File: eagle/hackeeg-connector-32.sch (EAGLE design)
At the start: 58 parts

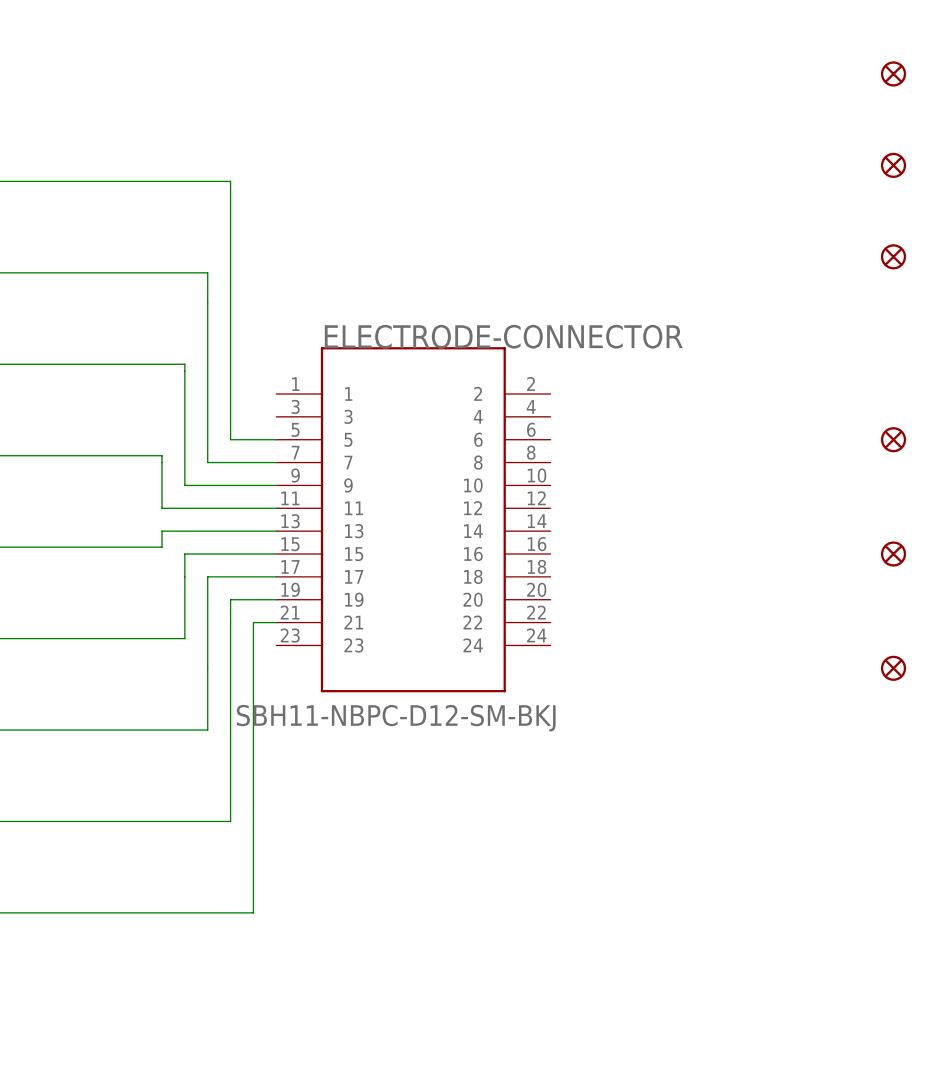
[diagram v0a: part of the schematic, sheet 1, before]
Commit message: connected IN1-8N to ground
- for cable noise reduction
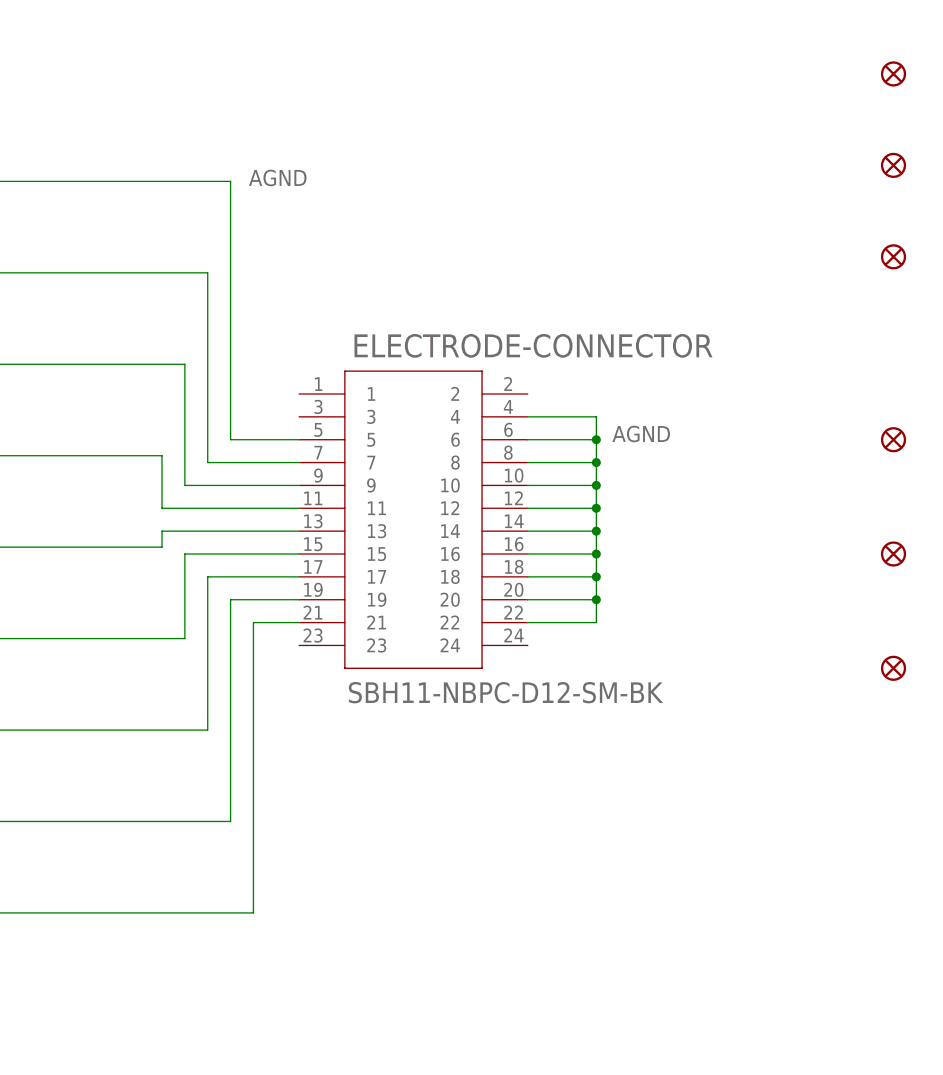
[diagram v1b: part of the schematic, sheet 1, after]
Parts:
- ELECTRODE-CONNECTOR, ELECTRODE-CONNECTOR1, ELECTRODE-CONNECTOR2, ELECTRODE-CONNECTOR3: value SBH11-NBPC-D12-SM-BKJ -> SBH11-NBPC-D12-SM-BK; device SBH11-NBPC-D12-SM-BK:SBH11-NBPC-D12-SM-BKJ -> SBH11-NBPC-D12-SM-BK:SBH11-NBPC-D12-SM-BK
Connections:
- removed net N$1: AGND.SIGNAL, ELECTRODE-CONNECTOR.5
- removed net N$10: AGND1.SIGNAL, ELECTRODE-CONNECTOR1.5
- removed net N$19: AGND2.SIGNAL, ELECTRODE-CONNECTOR2.5
- removed net N$28: AGND3.SIGNAL, ELECTRODE-CONNECTOR3.5
- new net AGND: AGND.SIGNAL, AGND1.SIGNAL, AGND2.SIGNAL, AGND3.SIGNAL, ELECTRODE-CONNECTOR.10, ELECTRODE-CONNECTOR.12, ELECTRODE-CONNECTOR.14, ELECTRODE-CONNECTOR.16, ELECTRODE-CONNECTOR.18, ELECTRODE-CONNECTOR.20, ELECTRODE-CONNECTOR.22, ELECTRODE-CONNECTOR.4, ELECTRODE-CONNECTOR.5, ELECTRODE-CONNECTOR.6, ELECTRODE-CONNECTOR.8, ELECTRODE-CONNECTOR1.10, ELECTRODE-CONNECTOR1.12, ELECTRODE-CONNECTOR1.14, ELECTRODE-CONNECTOR1.16, ELECTRODE-CONNECTOR1.18, ELECTRODE-CONNECTOR1.20, ELECTRODE-CONNECTOR1.22, ELECTRODE-CONNECTOR1.4, ELECTRODE-CONNECTOR1.5, ELECTRODE-CONNECTOR1.6, ELECTRODE-CONNECTOR1.8, ELECTRODE-CONNECTOR2.10, ELECTRODE-CONNECTOR2.12, ELECTRODE-CONNECTOR2.14, ELECTRODE-CONNECTOR2.16, ELECTRODE-CONNECTOR2.18, ELECTRODE-CONNECTOR2.20, ELECTRODE-CONNECTOR2.22, ELECTRODE-CONNECTOR2.4, ELECTRODE-CONNECTOR2.5, ELECTRODE-CONNECTOR2.6, ELECTRODE-CONNECTOR2.8, ELECTRODE-CONNECTOR3.10, ELECTRODE-CONNECTOR3.12, ELECTRODE-CONNECTOR3.14, ELECTRODE-CONNECTOR3.16, ELECTRODE-CONNECTOR3.18, ELECTRODE-CONNECTOR3.20, ELECTRODE-CONNECTOR3.22, ELECTRODE-CONNECTOR3.4, ELECTRODE-CONNECTOR3.5, ELECTRODE-CONNECTOR3.6, ELECTRODE-CONNECTOR3.8

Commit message: updated libraries to current
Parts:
- AGND, AGND1, AGND2, AGND3, IN1P, IN1P1, IN1P2, IN1P3, IN2P, IN2P1, IN2P2, IN2P3, IN3P, IN3P1, IN3P2, IN3P3, IN4P, IN4P1, IN4P2, IN4P3, IN5P, IN5P1, IN5P2, IN5P3, IN6P, IN6P1, IN6P2, IN6P3, IN7P, IN7P1, IN7P2, IN7P3, IN8P, IN8P1, IN8P2, IN8P3: value PO37729HEX-100 -> PO37729HEX-110; device po-37729:PO37729HEX-100 -> po-37729:PO37729HEX-110
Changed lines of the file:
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@@
 </classes>
 <parts>
-<part name="IN1P" library="po-37729" deviceset="PO37729" device="HEX-100"/>
+<part name="IN1P" library="po-37729" deviceset="PO37729" device="HEX-110"/>
 <part name="FRAME1" library="SparkFun-Aesthetics" library_urn="urn:adsk.eagle:library:507" deviceset="FRAME-LETTER" device="" package3d_urn="urn:adsk.eagle:package:37121/1"/>
 <part name="ELECTRODE-CONNECTOR" library="SBH11-NBPC-D12-SM-BK" deviceset="SBH11-NBPC-D12-SM-BK" device=""/>
 <part name="U$13" library="creative-commons" deviceset="CC-BY-SA" device=""/>
-<part name="IN2P" library="po-37729" deviceset="PO37729" device="HEX-100"/>
-<part name="IN3P" library="po-37729" deviceset="PO37729" device="HEX-100"/>
-<part name="IN4P" library="po-37729" deviceset="PO37729" device="HEX-100"/>
-<part name="IN5P" library="po-37729" deviceset="PO37729" device="HEX-100"/>
-<part name="IN6P" library="po-37729" deviceset="PO37729" device="HEX-100"/>
-<part name="IN7P" library="po-37729" deviceset="PO37729" device="HEX-100"/>
-<part name="AGND" library="po-37729" deviceset="PO37729" device="HEX-100"/>
-<part name="IN8P" library="po-37729" deviceset="PO37729" device="HEX-100"/>
+<part name="IN2P" library="po-37729" deviceset="PO37729" device="HEX-110"/>
+<part name="IN3P" library="po-37729" deviceset="PO37729" device="HEX-110"/>
+<part name="IN4P" library="po-37729" deviceset="PO37729" device="HEX-110"/>
+<part name="IN5P" library="po-37729" deviceset="PO37729" device="HEX-110"/>
+<part name="IN6P" library="po-37729" deviceset="PO37729" device="HEX-110"/>
+<part name="IN7P" library="po-37729" deviceset="PO37729" device="HEX-110"/>
+<part name="AGND" library="po-37729" deviceset="PO37729" device="HEX-110"/>
+<part name="IN8P" library="po-37729" deviceset="PO37729" device="HEX-110"/>
 <part name="U$1" library="endless-knot" deviceset="ENDLESSKNOT" device="ENDLESSKNOT-MEDIUM"/>
-<part name="IN1P1" library="po-37729" deviceset="PO37729" device="HEX-100"/>
+<part name="IN1P1" library="po-37729" deviceset="PO37729" device="HEX-110"/>
 <part name="FRAME2" library="SparkFun-Aesthetics" library_urn="urn:adsk.eagle:library:507" deviceset="FRAME-LETTER" device="" package3d_urn="urn:adsk.eagle:package:37121/1"/>
 <part name="ELECTRODE-CONNECTOR1" library="SBH11-NBPC-D12-SM-BK" deviceset="SBH11-NBPC-D12-SM-BK" device=""/>
 <part name="U$2" library="creative-commons" deviceset="CC-BY-SA" device=""/>
-<part name="IN2P1" library="po-37729" deviceset="PO37729" device="HEX-100"/>
-<part name="IN3P1" library="po-37729" deviceset="PO37729" device="HEX-100"/>
-<part name="IN4P1" library="po-37729" deviceset="PO37729" device="HEX-100"/>
-<part name="IN5P1" library="po-37729" deviceset="PO37729" device="HEX-100"/>
-<part name="IN6P1" library="po-37729" deviceset="PO37729" device="HEX-100"/>
-<part name="IN7P1" library="po-37729" deviceset="PO37729" device="HEX-100"/>
-<part name="AGND1" library="po-37729" deviceset="PO37729" device="HEX-100"/>
-<part name="IN8P1" library="po-37729" deviceset="PO37729" device="HEX-100"/>
+<part name="IN2P1" library="po-37729" deviceset="PO37729" device="HEX-110"/>
+<part name="IN3P1" library="po-37729" deviceset="PO37729" device="HEX-110"/>
+<part name="IN4P1" library="po-37729" deviceset="PO37729" device="HEX-110"/>
+<part name="IN5P1" library="po-37729" deviceset="PO37729" device="HEX-110"/>
+<part name="IN6P1" library="po-37729" deviceset="PO37729" device="HEX-110"/>
+<part name="IN7P1" library="po-37729" deviceset="PO37729" device="HEX-110"/>
+<part name="AGND1" library="po-37729" deviceset="PO37729" device="HEX-110"/>
+<part name="IN8P1" library="po-37729" deviceset="PO37729" device="HEX-110"/>
 <part name="U$3" library="endless-knot" deviceset="ENDLESSKNOT" device="ENDLESSKNOT-MEDIUM"/>
-<part name="IN1P2" library="po-37729" deviceset="PO37729" device="HEX-100"/>
+<part name="IN1P2" library="po-37729" deviceset="PO37729" device="HEX-110"/>
 <part name="FRAME3" library="SparkFun-Aesthetics" library_urn="urn:adsk.eagle:library:507" deviceset="FRAME-LETTER" device="" package3d_urn="urn:adsk.eagle:package:37121/1"/>
 <part name="ELECTRODE-CONNECTOR2" library="SBH11-NBPC-D12-SM-BK" deviceset="SBH11-NBPC-D12-SM-BK" device=""/>
 <part name="U$4" library="creative-commons" deviceset="CC-BY-SA" device=""/>
-<part name="IN2P2" library="po-37729" deviceset="PO37729" device="HEX-100"/>
-<part name="IN3P2" library="po-37729" deviceset="PO37729" device="HEX-100"/>
-<part name="IN4P2" library="po-37729" deviceset="PO37729" device="HEX-100"/>
-<part name="IN5P2" library="po-37729" deviceset="PO37729" device="HEX-100"/>
-<part name="IN6P2" library="po-37729" deviceset="PO37729" device="HEX-100"/>
-<part name="IN7P2" library="po-37729" deviceset="PO37729" device="HEX-100"/>
-<part name="AGND2" library="po-37729" deviceset="PO37729" device="HEX-100"/>
-<part name="IN8P2" library="po-37729" deviceset="PO37729" device="HEX-100"/>
+<part name="IN2P2" library="po-37729" deviceset="PO37729" device="HEX-110"/>
+<part name="IN3P2" library="po-37729" deviceset="PO37729" device="HEX-110"/>
+<part name="IN4P2" library="po-37729" deviceset="PO37729" device="HEX-110"/>
+<part name="IN5P2" library="po-37729" deviceset="PO37729" device="HEX-110"/>
+<part name="IN6P2" library="po-37729" deviceset="PO37729" device="HEX-110"/>
+<part name="IN7P2" library="po-37729" deviceset="PO37729" device="HEX-110"/>
+<part name="AGND2" library="po-37729" deviceset="PO37729" device="HEX-110"/>
+<part name="IN8P2" library="po-37729" deviceset="PO37729" device="HEX-110"/>
 <part name="U$5" library="endless-knot" deviceset="ENDLESSKNOT" device="ENDLESSKNOT-MEDIUM"/>
-<part name="IN1P3" library="po-37729" deviceset="PO37729" device="HEX-100"/>
+<part name="IN1P3" library="po-37729" deviceset="PO37729" device="HEX-110"/>
 <part name="FRAME4" library="SparkFun-Aesthetics" library_urn="urn:adsk.eagle:library:507" deviceset="FRAME-LETTER" device="" package3d_urn="urn:adsk.eagle:package:37121/1"/>
 <part name="ELECTRODE-CONNECTOR3" library="SBH11-NBPC-D12-SM-BK" deviceset="SBH11-NBPC-D12-SM-BK" device=""/>
 <part name="U$6" library="creative-commons" deviceset="CC-BY-SA" device=""/>
-<part name="IN2P3" library="po-37729" deviceset="PO37729" device="HEX-100"/>
-<part name="IN3P3" library="po-37729" deviceset="PO37729" device="HEX-100"/>
-<part name="IN4P3" library="po-37729" deviceset="PO37729" device="HEX-100"/>
-<part name="IN5P3" library="po-37729" deviceset="PO37729" device="HEX-100"/>
-<part name="IN6P3" library="po-37729" deviceset="PO37729" device="HEX-100"/>
-<part name="IN7P3" library="po-37729" deviceset="PO37729" device="HEX-100"/>
-<part name="AGND3" library="po-37729" deviceset="PO37729" device="HEX-100"/>
-<part name="IN8P3" library="po-37729" deviceset="PO37729" device="HEX-100"/>
+<part name="IN2P3" library="po-37729" deviceset="PO37729" device="HEX-110"/>
+<part name="IN3P3" library="po-37729" deviceset="PO37729" device="HEX-110"/>
+<part name="IN4P3" library="po-37729" deviceset="PO37729" device="HEX-110"/>
+<part name="IN5P3" library="po-37729" deviceset="PO37729" device="HEX-110"/>
+<part name="IN6P3" library="po-37729" deviceset="PO37729" device="HEX-110"/>
+<part name="IN7P3" library="po-37729" deviceset="PO37729" device="HEX-110"/>
+<part name="AGND3" library="po-37729" deviceset="PO37729" device="HEX-110"/>
+<part name="IN8P3" library="po-37729" deviceset="PO37729" device="HEX-110"/>
 <part name="U$7" library="endless-knot" deviceset="ENDLESSKNOT" device="ENDLESSKNOT-MEDIUM"/>
 <part name="FD1" library="SparkFun-Aesthetics" library_urn="urn:adsk.eagle:library:507" deviceset="FIDUCIAL" device="1X2" package3d_urn="urn:adsk.eagle:package:37108/1"/>

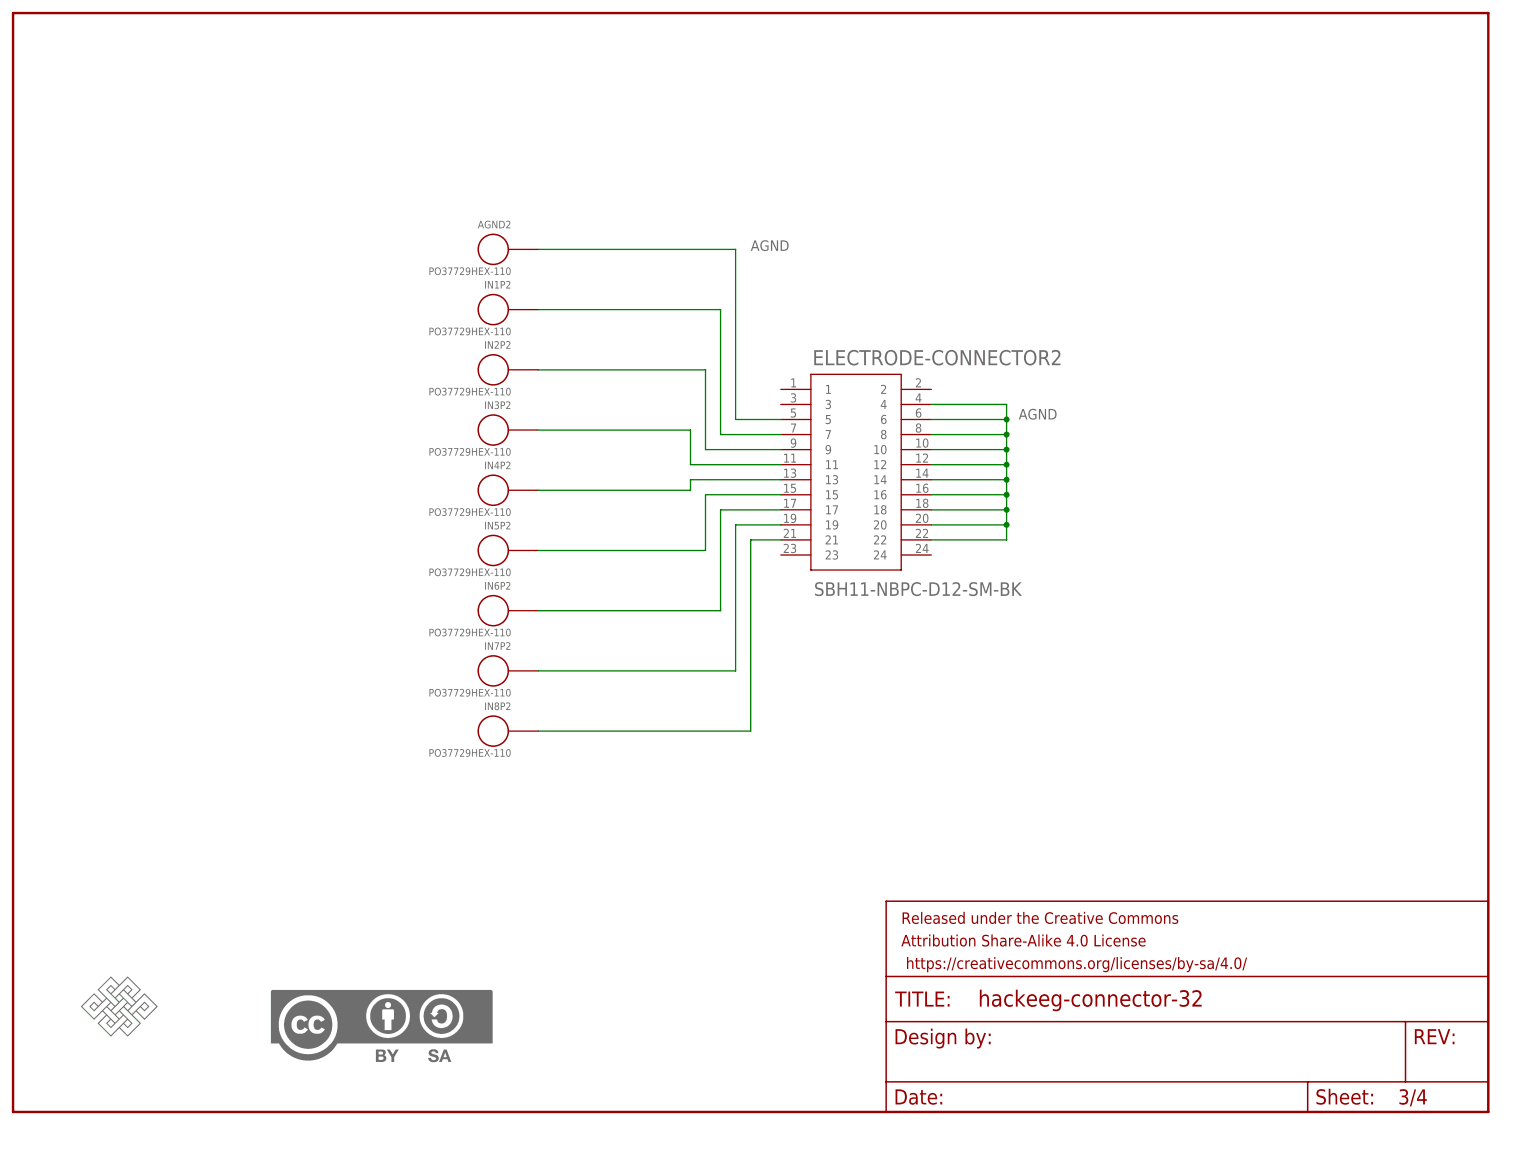
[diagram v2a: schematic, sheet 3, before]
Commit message: relicense to CERN OHL 1.2 - sch
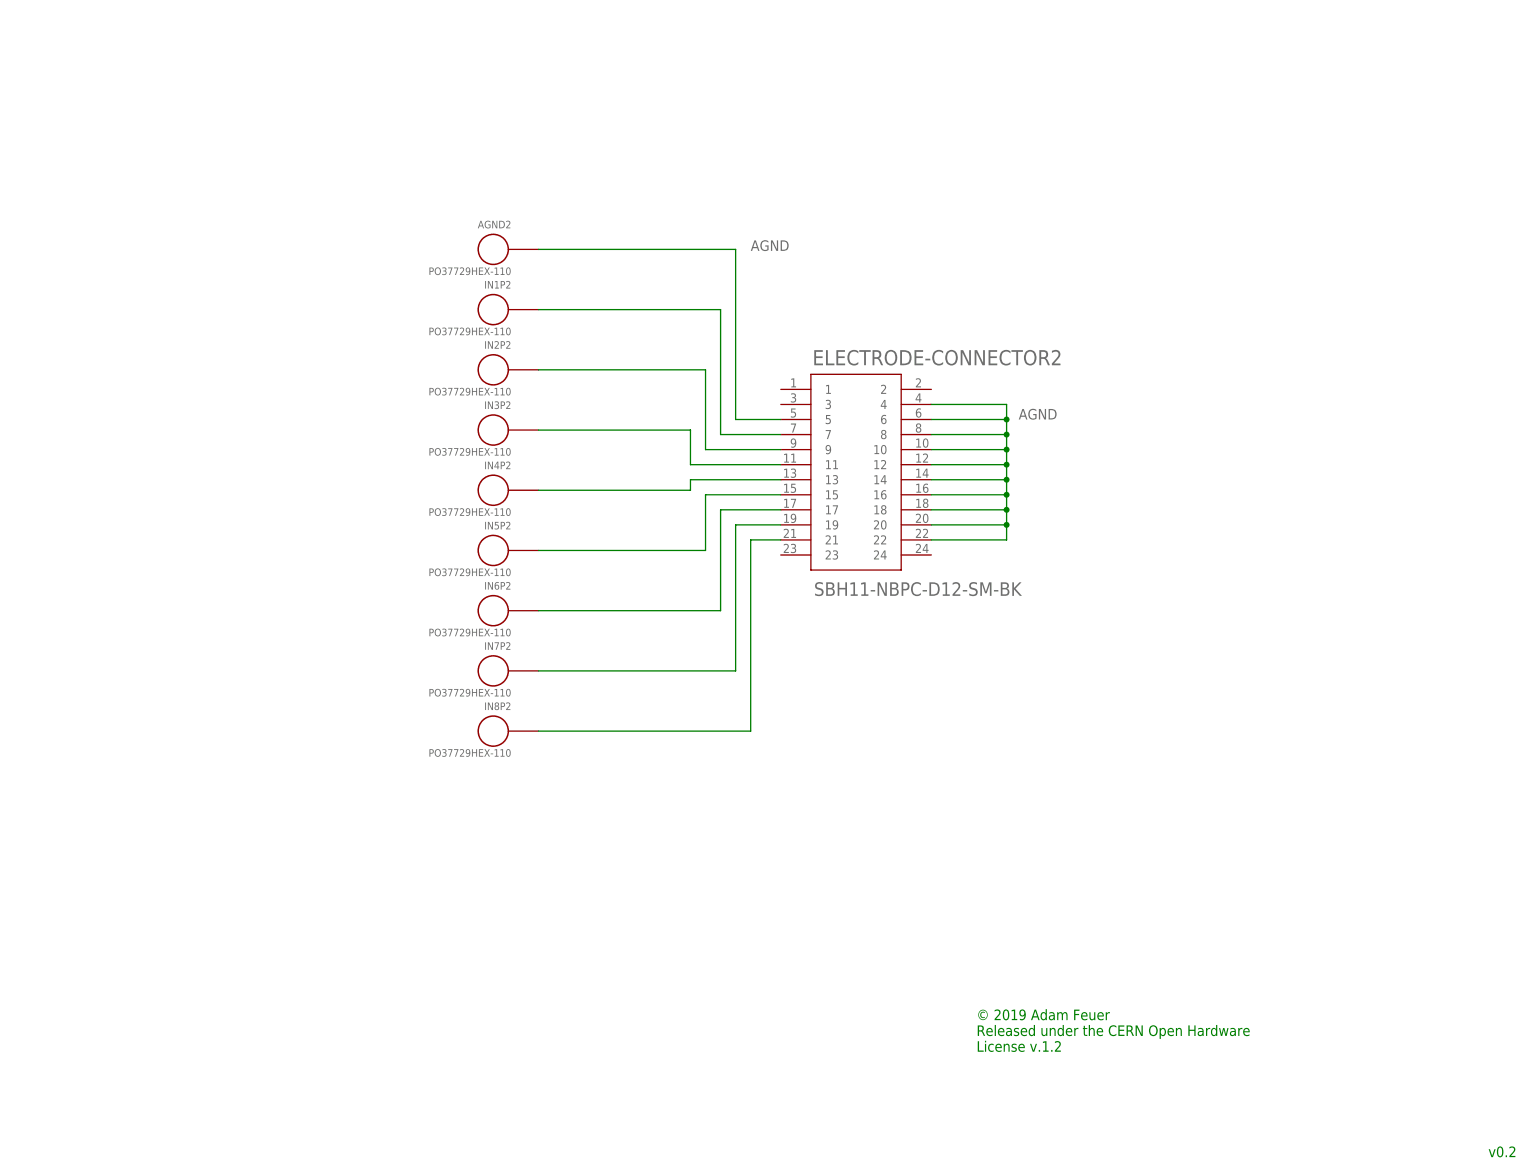
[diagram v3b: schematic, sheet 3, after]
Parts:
- removed FRAME1, FRAME2, FRAME3, FRAME4: FRAME-LETTER, SparkFun-Aesthetics:FRAME-LETTER
- removed U$13, U$2, U$4, U$6: CC-BY-SA, creative-commons:CC-BY-SA
- removed U$3, U$5, U$7: ENDLESSKNOTENDLESSKNOT-MEDIUM, endless-knot:ENDLESSKNOTENDLESSKNOT-MEDIUM
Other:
- note added: "v0.2"
- note added: "© 2019 Adam Feuer Released under the CERN Open Hardware License v.1.2"
